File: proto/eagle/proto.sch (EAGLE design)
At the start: 40 parts, among them U1 ARDUINO_MINI_PRO, U2 ATA6663, U3 7805T, U4 FTDI-BOARD

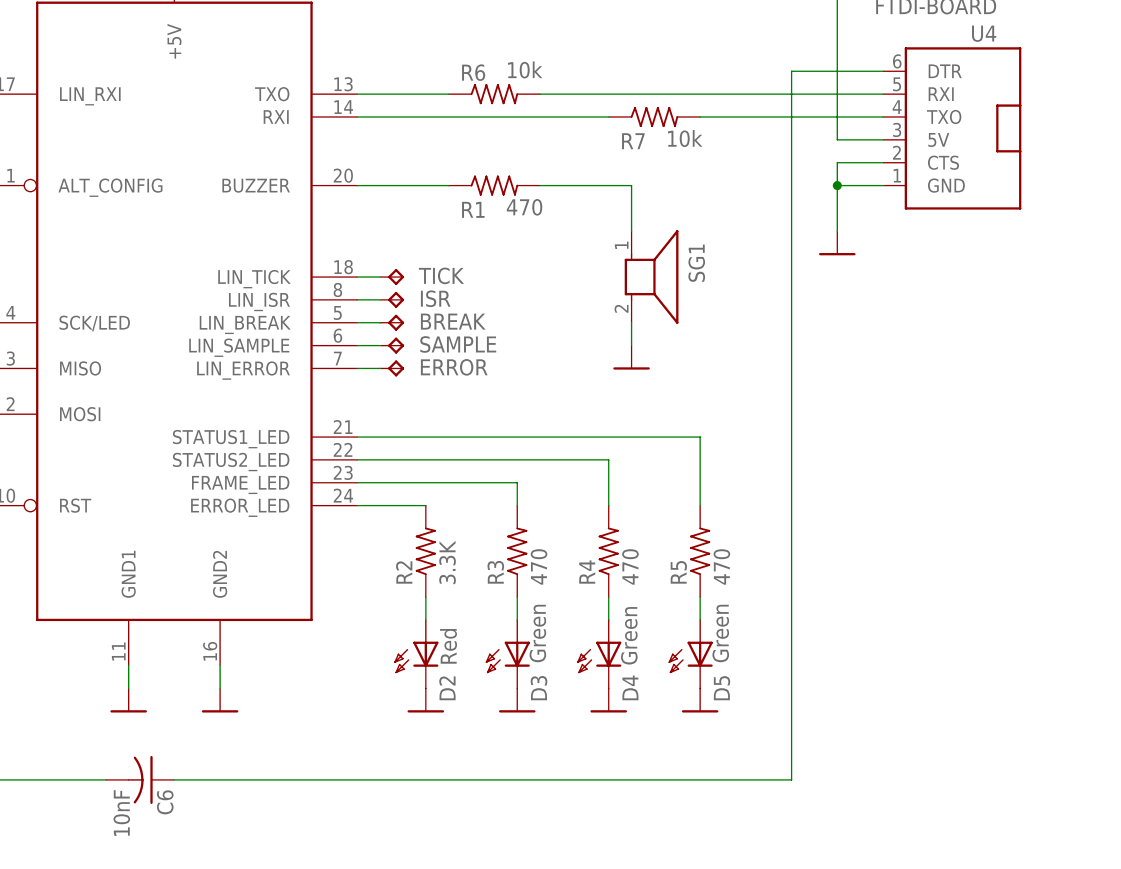
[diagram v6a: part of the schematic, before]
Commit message: Added buzzer output. Cleaned up enums (changed from sing16 to uing8).
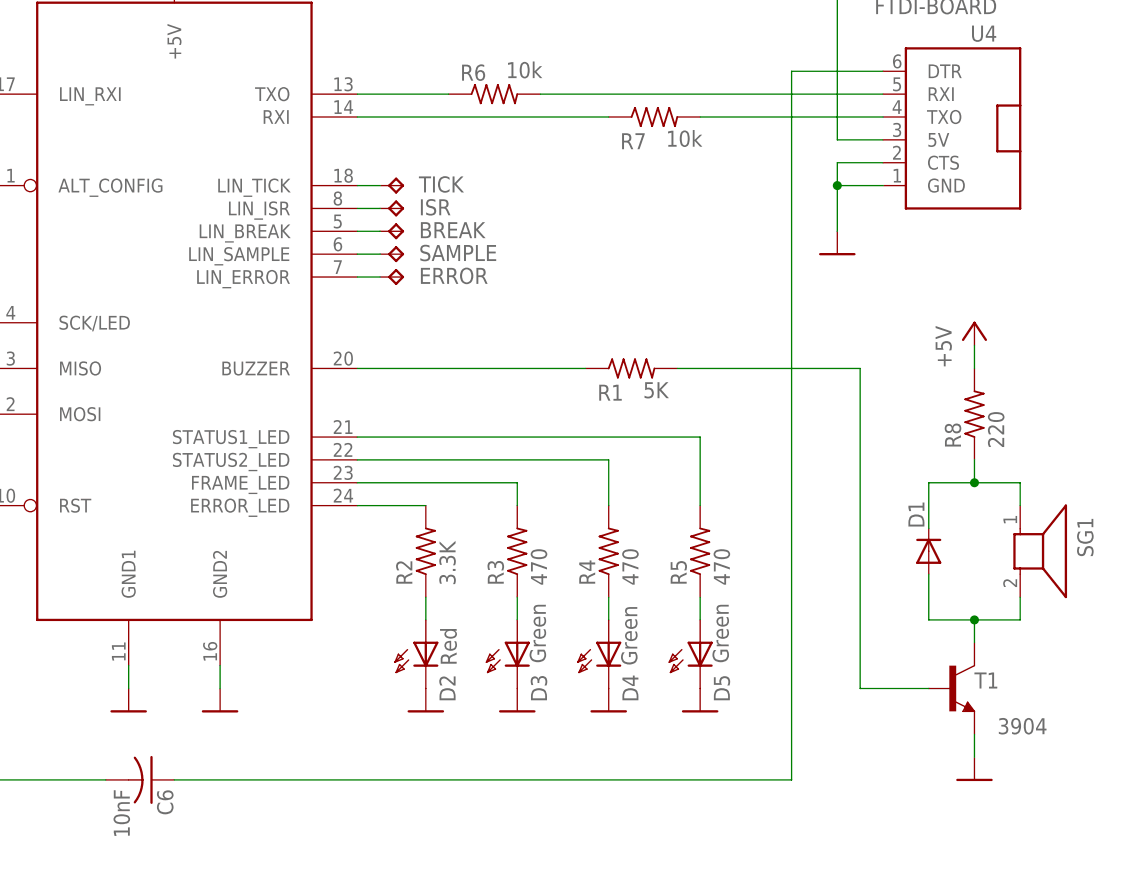
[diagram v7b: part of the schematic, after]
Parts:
- added D1: (no value), diode:DIODE-MINIMELF
- added R8: 220, rcl:R-US_R0805
- added T1: 3904, transistor:MMBT3904LT1-NPN-SOT23-BEC
- R1: value 470 -> 5K
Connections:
- new net N$30: D1.C, R8.1, SG1.1
- new net N$31: D1.A, SG1.2, T1.C
- net +5V: now also R8.2
- net GND: now also T1.E; no longer SG1.2
- net N$19: now also T1.B; no longer SG1.1
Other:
- moved on the sheet: BREAK, ERROR, ISR, R1, SAMPLE, SG1, TICK
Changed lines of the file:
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@@
 <part name="ISR" library="testpad" deviceset="TP" device="PAD1-17"/>
 <part name="SG1" library="buzzer" deviceset="F/SMX" device="" value=""/>
+<part name="R1" library="rcl" deviceset="R-US_" device="R0805" value="5K"/>
+<part name="T1" library="transistor" deviceset="*-NPN-" device="SOT23-BEC" technology="MMBT3904LT1" value="3904"/>
 <part name="GND18" library="my_lib" deviceset="GND" device=""/>
-<part name="R1" library="rcl" deviceset="R-US_" device="R0805" value="470"/>
+<part name="D1" library="diode" deviceset="DIODE-" device="MINIMELF"/>
+<part name="P+3" library="supply1" deviceset="+5V" device=""/>
+<part name="R8" library="rcl" deviceset="R-US_" device="R0805" value="220"/>
 </parts>
 <sheets>
@@
 <attribute name="VALUE" x="243.586" y="204.089" size="1.778" layer="96" rot="R180"/>
 </instance>
-<instance part="TICK" gate="G$1" x="226.06" y="127" smashed="yes" rot="R270">
-<attribute name="NAME" x="227.838" y="126.238" size="1.778" layer="95"/>
-<attribute name="TP_SIGNAL_NAME" x="224.79" y="125.73" size="1.778" layer="97" rot="R270"/>
+<instance part="TICK" gate="G$1" x="226.06" y="137.16" smashed="yes" rot="R270">
+<attribute name="NAME" x="227.838" y="136.398" size="1.778" layer="95"/>
+<attribute name="TP_SIGNAL_NAME" x="224.79" y="135.89" size="1.778" layer="97" rot="R270"/>
 </instance>
 <instance part="LED" gate="G$1" x="144.78" y="129.54" smashed="yes">
@@
 <instance part="GND15" gate="1" x="259.08" y="78.74"/>
 <instance part="P+4" gate="1" x="137.16" y="165.1"/>
-<instance part="BREAK" gate="G$1" x="226.06" y="121.92" smashed="yes" rot="R270">
-<attribute name="NAME" x="227.838" y="121.158" size="1.778" layer="95"/>
-<attribute name="TP_SIGNAL_NAME" x="224.79" y="120.65" size="1.778" layer="97" rot="R270"/>
-</instance>
-<instance part="SAMPLE" gate="G$1" x="226.06" y="119.38" smashed="yes" rot="R270">
-<attribute name="NAME" x="227.838" y="118.618" size="1.778" layer="95"/>
-<attribute name="TP_SIGNAL_NAME" x="224.79" y="118.11" size="1.778" layer="97" rot="R270"/>
-</instance>
-<instance part="ERROR" gate="G$1" x="226.06" y="116.84" smashed="yes" rot="R270">
-<attribute name="NAME" x="227.838" y="116.078" size="1.778" layer="95"/>
-<attribute name="TP_SIGNAL_NAME" x="224.79" y="115.57" size="1.778" layer="97" rot="R270"/>
+<instance part="BREAK" gate="G$1" x="226.06" y="132.08" smashed="yes" rot="R270">
+<attribute name="NAME" x="227.838" y="131.318" size="1.778" layer="95"/>
+<attribute name="TP_SIGNAL_NAME" x="224.79" y="130.81" size="1.778" layer="97" rot="R270"/>
+</instance>
+<instance part="SAMPLE" gate="G$1" x="226.06" y="129.54" smashed="yes" rot="R270">
+<attribute name="NAME" x="227.838" y="128.778" size="1.778" layer="95"/>
+<attribute name="TP_SIGNAL_NAME" x="224.79" y="128.27" size="1.778" layer="97" rot="R270"/>
+</instance>
+<instance part="ERROR" gate="G$1" x="226.06" y="127" smashed="yes" rot="R270">
+<attribute name="NAME" x="227.838" y="126.238" size="1.778" layer="95"/>
+<attribute name="TP_SIGNAL_NAME" x="224.79" y="125.73" size="1.778" layer="97" rot="R270"/>
 </instance>
 <instance part="GND16" gate="1" x="205.74" y="78.74"/>
@@
 <instance part="S1" gate="1" x="172.72" y="137.16" rot="R270"/>
 <instance part="GND17" gate="1" x="165.1" y="132.08"/>
-<instance part="ISR" gate="G$1" x="226.06" y="124.46" smashed="yes" rot="R270">
-<attribute name="NAME" x="227.838" y="123.698" size="1.778" layer="95"/>
-<attribute name="TP_SIGNAL_NAME" x="224.79" y="123.19" size="1.778" layer="97" rot="R270"/>
-</instance>
-<instance part="SG1" gate="G$1" x="251.46" y="127" rot="R270"/>
-<instance part="GND18" gate="1" x="251.46" y="116.84"/>
-<instance part="R1" gate="G$1" x="236.22" y="137.16" smashed="yes">
-<attribute name="NAME" x="232.41" y="133.5786" size="1.778" layer="95"/>
-<attribute name="VALUE" x="237.49" y="133.858" size="1.778" layer="96"/>
-</instance>
+<instance part="ISR" gate="G$1" x="226.06" y="134.62" smashed="yes" rot="R270">
+<attribute name="NAME" x="227.838" y="133.858" size="1.778" layer="95"/>
+<attribute name="TP_SIGNAL_NAME" x="224.79" y="133.35" size="1.778" layer="97" rot="R270"/>
+</instance>
+<instance part="SG1" gate="G$1" x="294.64" y="96.52" rot="R270"/>
+<instance part="R1" gate="G$1" x="251.46" y="116.84" smashed="yes">
+<attribute name="NAME" x="247.65" y="113.2586" size="1.778" layer="95"/>
+<attribute name="VALUE" x="252.73" y="113.538" size="1.778" layer="96"/>
+</instance>
+<instance part="T1" gate="G$1" x="287.02" y="81.28" smashed="yes">
+<attribute name="NAME" x="289.56" y="81.28" size="1.778" layer="95"/>
+<attribute name="VALUE" x="292.1" y="76.2" size="1.778" layer="96"/>
+</instance>
+<instance part="GND18" gate="1" x="289.56" y="71.12"/>
+<instance part="D1" gate="G$1" x="284.48" y="96.52" rot="R90"/>
+<instance part="P+3" gate="1" x="289.56" y="121.92"/>
+<instance part="R8" gate="G$1" x="289.56" y="111.76" rot="R90"/>
 </instances>
 <busses>
@@
 </segment>
 <segment>
-<pinref part="SG1" gate="G$1" pin="2"/>
+<pinref part="T1" gate="G$1" pin="E"/>
 <pinref part="GND18" gate="1" pin="GND"/>
-<wire x1="251.46" y1="121.92" x2="251.46" y2="119.38" width="0.1524" layer="91"/>
+<wire x1="289.56" y1="76.2" x2="289.56" y2="73.66" width="0.1524" layer="91"/>
 </segment>
 </net>
@@
 <wire x1="129.54" y1="88.9" x2="129.54" y2="93.98" width="0.1524" layer="91"/>
 </segment>
+<segment>
+<pinref part="P+3" gate="1" pin="+5V"/>
+<pinref part="R8" gate="G$1" pin="2"/>
+<wire x1="289.56" y1="119.38" x2="289.56" y2="116.84" width="0.1524" layer="91"/>
+</segment>
 </net>
 <net name="N$14" class="0">
@@
 <pinref part="U1" gate="G$1" pin="LIN_TICK"/>
 <pinref part="TICK" gate="G$1" pin="TP"/>
-<wire x1="223.52" y1="127" x2="220.98" y2="127" width="0.1524" layer="91"/>
+<wire x1="223.52" y1="137.16" x2="220.98" y2="137.16" width="0.1524" layer="91"/>
 </segment>
 </net>
@@
 <pinref part="U1" gate="G$1" pin="LIN_BREAK"/>
 <pinref part="BREAK" gate="G$1" pin="TP"/>
-<wire x1="220.98" y1="121.92" x2="223.52" y2="121.92" width="0.1524" layer="91"/>
+<wire x1="220.98" y1="132.08" x2="223.52" y2="132.08" width="0.1524" layer="91"/>
 </segment>
 </net>
@@
 <pinref part="U1" gate="G$1" pin="LIN_SAMPLE"/>
 <pinref part="SAMPLE" gate="G$1" pin="TP"/>
-<wire x1="220.98" y1="119.38" x2="223.52" y2="119.38" width="0.1524" layer="91"/>
+<wire x1="220.98" y1="129.54" x2="223.52" y2="129.54" width="0.1524" layer="91"/>
 </segment>
 </net>
@@
 <pinref part="U1" gate="G$1" pin="LIN_ERROR"/>
 <pinref part="ERROR" gate="G$1" pin="TP"/>
-<wire x1="220.98" y1="116.84" x2="223.52" y2="116.84" width="0.1524" layer="91"/>
+<wire x1="220.98" y1="127" x2="223.52" y2="127" width="0.1524" layer="91"/>
 </segment>
 </net>
@@
 <pinref part="U1" gate="G$1" pin="LIN_ISR"/>
 <pinref part="ISR" gate="G$1" pin="TP"/>
-<wire x1="220.98" y1="124.46" x2="223.52" y2="124.46" width="0.1524" layer="91"/>
+<wire x1="220.98" y1="134.62" x2="223.52" y2="134.62" width="0.1524" layer="91"/>
+</segment>
+</net>
+<net name="N$31" class="0">
+<segment>
+<pinref part="D1" gate="G$1" pin="A"/>
+<wire x1="284.48" y1="93.98" x2="284.48" y2="88.9" width="0.1524" layer="91"/>
+<pinref part="T1" gate="G$1" pin="C"/>
+<wire x1="284.48" y1="88.9" x2="289.56" y2="88.9" width="0.1524" layer="91"/>
+<wire x1="289.56" y1="88.9" x2="289.56" y2="86.36" width="0.1524" layer="91"/>
+<pinref part="SG1" gate="G$1" pin="2"/>
+<wire x1="289.56" y1="88.9" x2="294.64" y2="88.9" width="0.1524" layer="91"/>
+<wire x1="294.64" y1="88.9" x2="294.64" y2="91.44" width="0.1524" layer="91"/>
+<junction x="289.56" y="88.9"/>
 </segment>
 </net>
@@
 <pinref part="U1" gate="G$1" pin="BUZZER"/>
 <pinref part="R1" gate="G$1" pin="1"/>
-<wire x1="220.98" y1="137.16" x2="231.14" y2="137.16" width="0.1524" layer="91"/>
+<wire x1="220.98" y1="116.84" x2="246.38" y2="116.84" width="0.1524" layer="91"/>
 </segment>
 </net>
 <net name="N$19" class="0">
 <segment>
+<pinref part="T1" gate="G$1" pin="B"/>
+<wire x1="284.48" y1="81.28" x2="276.86" y2="81.28" width="0.1524" layer="91"/>
+<wire x1="276.86" y1="81.28" x2="276.86" y2="116.84" width="0.1524" layer="91"/>
 <pinref part="R1" gate="G$1" pin="2"/>
+<wire x1="276.86" y1="116.84" x2="256.54" y2="116.84" width="0.1524" layer="91"/>
+</segment>
+</net>
+<net name="N$30" class="0">
+<segment>
+<pinref part="D1" gate="G$1" pin="C"/>
+<wire x1="284.48" y1="99.06" x2="284.48" y2="104.14" width="0.1524" layer="91"/>
 <pinref part="SG1" gate="G$1" pin="1"/>
-<wire x1="241.3" y1="137.16" x2="251.46" y2="137.16" width="0.1524" layer="91"/>
-<wire x1="251.46" y1="137.16" x2="251.46" y2="132.08" width="0.1524" layer="91"/>
-</segment>
-</net>
+<wire x1="284.48" y1="104.14" x2="289.56" y2="104.14" width="0.1524" layer="91"/>
+<wire x1="289.56" y1="104.14" x2="294.64" y2="104.14" width="0.1524" layer="91"/>
+<wire x1="294.64" y1="104.14" x2="294.64" y2="101.6" width="0.1524" layer="91"/>
+<pinref part="R8" gate="G$1" pin="1"/>
+<wire x1="289.56" y1="106.68" x2="289.56" y2="104.14" width="0.1524" layer="91"/>
+<junction x="289.56" y="104.14"/>
+</segment>
+</net>
